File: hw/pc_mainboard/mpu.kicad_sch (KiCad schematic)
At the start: 0 parts

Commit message: Added MPU information
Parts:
- added U1: STM32MP151AABx, Package_BGA:ST_LFBGA-354_16x16mm_Layout19x19_P0.8mm, symbol MCU_ST_STM32MP1:STM32MP151AABx
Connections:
- new net: U1.A1 (VSS), U1.A19 (VSS), U1.B2 (VSS), U1.B6 (VSS), U1.C12 (VSS), U1.C13 (VSS), U1.C14 (VSS), U1.C15 (VSS), U1.C16 (VSS), U1.C17 (VSS), U1.C3 (VSS), U1.D1 (VSS), U1.D4 (VSS), U1.D5 (VSS), U1.D8 (VSS), U1.E10 (VSS), U1.E12 (VSS), U1.E14 (VSS), U1.E16 (VSS), U1.E2 (VSS), U1.E4 (VSS), U1.E5 (VSS), U1.E6 (VSS), U1.E8 (VSS), U1.F11 (VSS), U1.F15 (VSS), U1.F5 (VSS), U1.F7 (VSS), U1.F9 (VSS), U1.G10 (VSS), U1.G12 (VSS), U1.G14 (VSS), U1.G2 (VSS), U1.G4 (VSS), U1.G6 (VSS), U1.G8 (VSS), U1.H11 (VSS), U1.H13 (VSS), U1.H15 (VSS), U1.H5 (VSS), U1.H7 (VSS), U1.H9 (VSS), U1.J10 (VSS), U1.J12 (VSS), U1.J14 (VSS), U1.J3 (VSS), U1.J6 (VSS), U1.J8 (VSS), U1.K11 (VSS), U1.K13 (VSS), U1.K15 (VSS), U1.K2 (VSS), U1.K5 (VSS), U1.K7 (VSS), U1.K9 (VSS), U1.L10 (VSS), U1.L12 (VSS), U1.L14 (VSS), U1.L6 (VSS), U1.L8 (VSS), U1.M11 (VSS), U1.M13 (VSS), U1.M15 (VSS), U1.M5 (VSS), U1.M7 (VSS), U1.M9 (VSS), U1.N10 (VSS), U1.N12 (VSS), U1.N14 (VSS), U1.N6 (VSS), U1.N8 (VSS), U1.P11 (VSS), U1.P13 (VSS), U1.P15 (VSS), U1.P7 (VSS), U1.P9 (VSS), U1.R10 (VSS), U1.R12 (VSS), U1.R14 (VSS), U1.R16 (VSS), U1.R2 (VSS), U1.R6 (VSS), U1.R8 (VSS), U1.T4 (VSS), U1.U17 (VSS), U1.U3 (VSS), U1.U6 (VSS), U1.U8 (VSS), U1.W1 (VSS), U1.W19 (VSS)
- new net: U1.N4 (VSSA), U1.P5 (VSSA), U1.R5 (VSSA)
- new net: U1.U13 (VSS_USBHS), U1.U14 (VSS_USBHS), U1.V12 (VSS_USBHS), U1.V15 (VSS_USBHS)
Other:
- title: (none) -> MPU

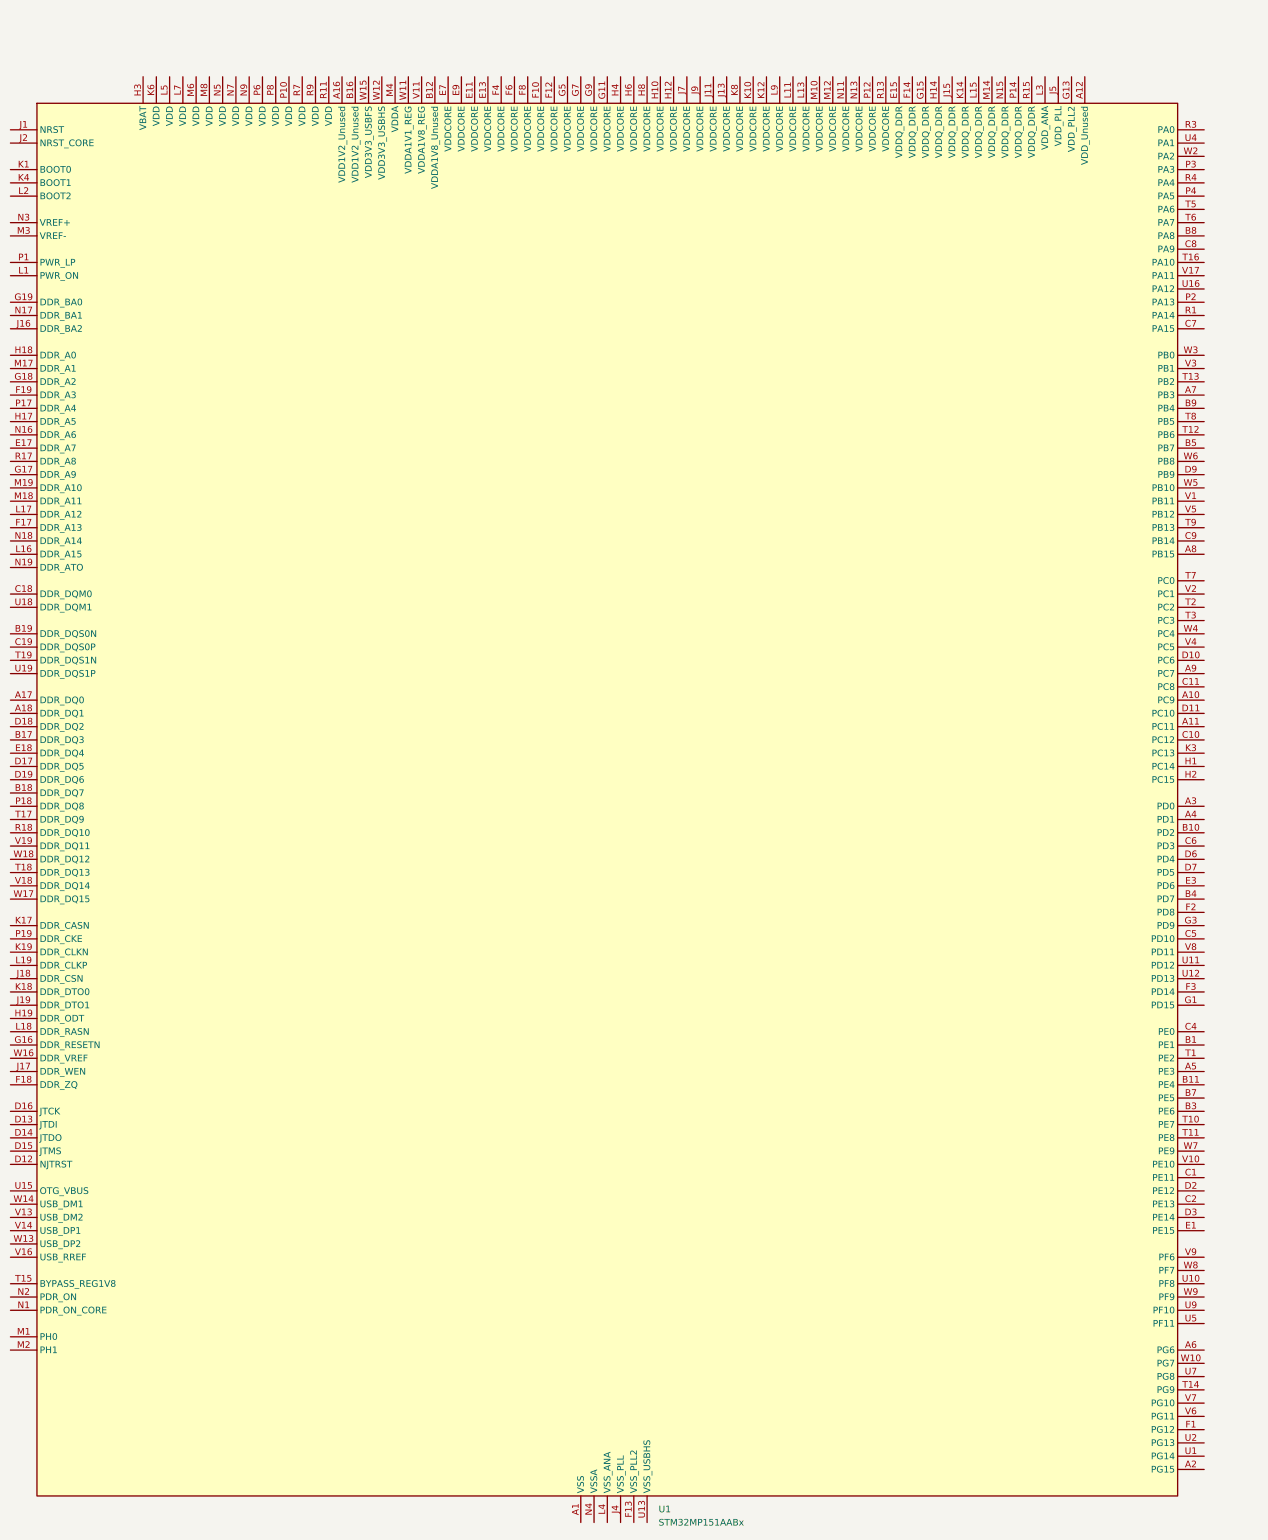
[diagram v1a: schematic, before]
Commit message: RAM Schematic Capture (#39)
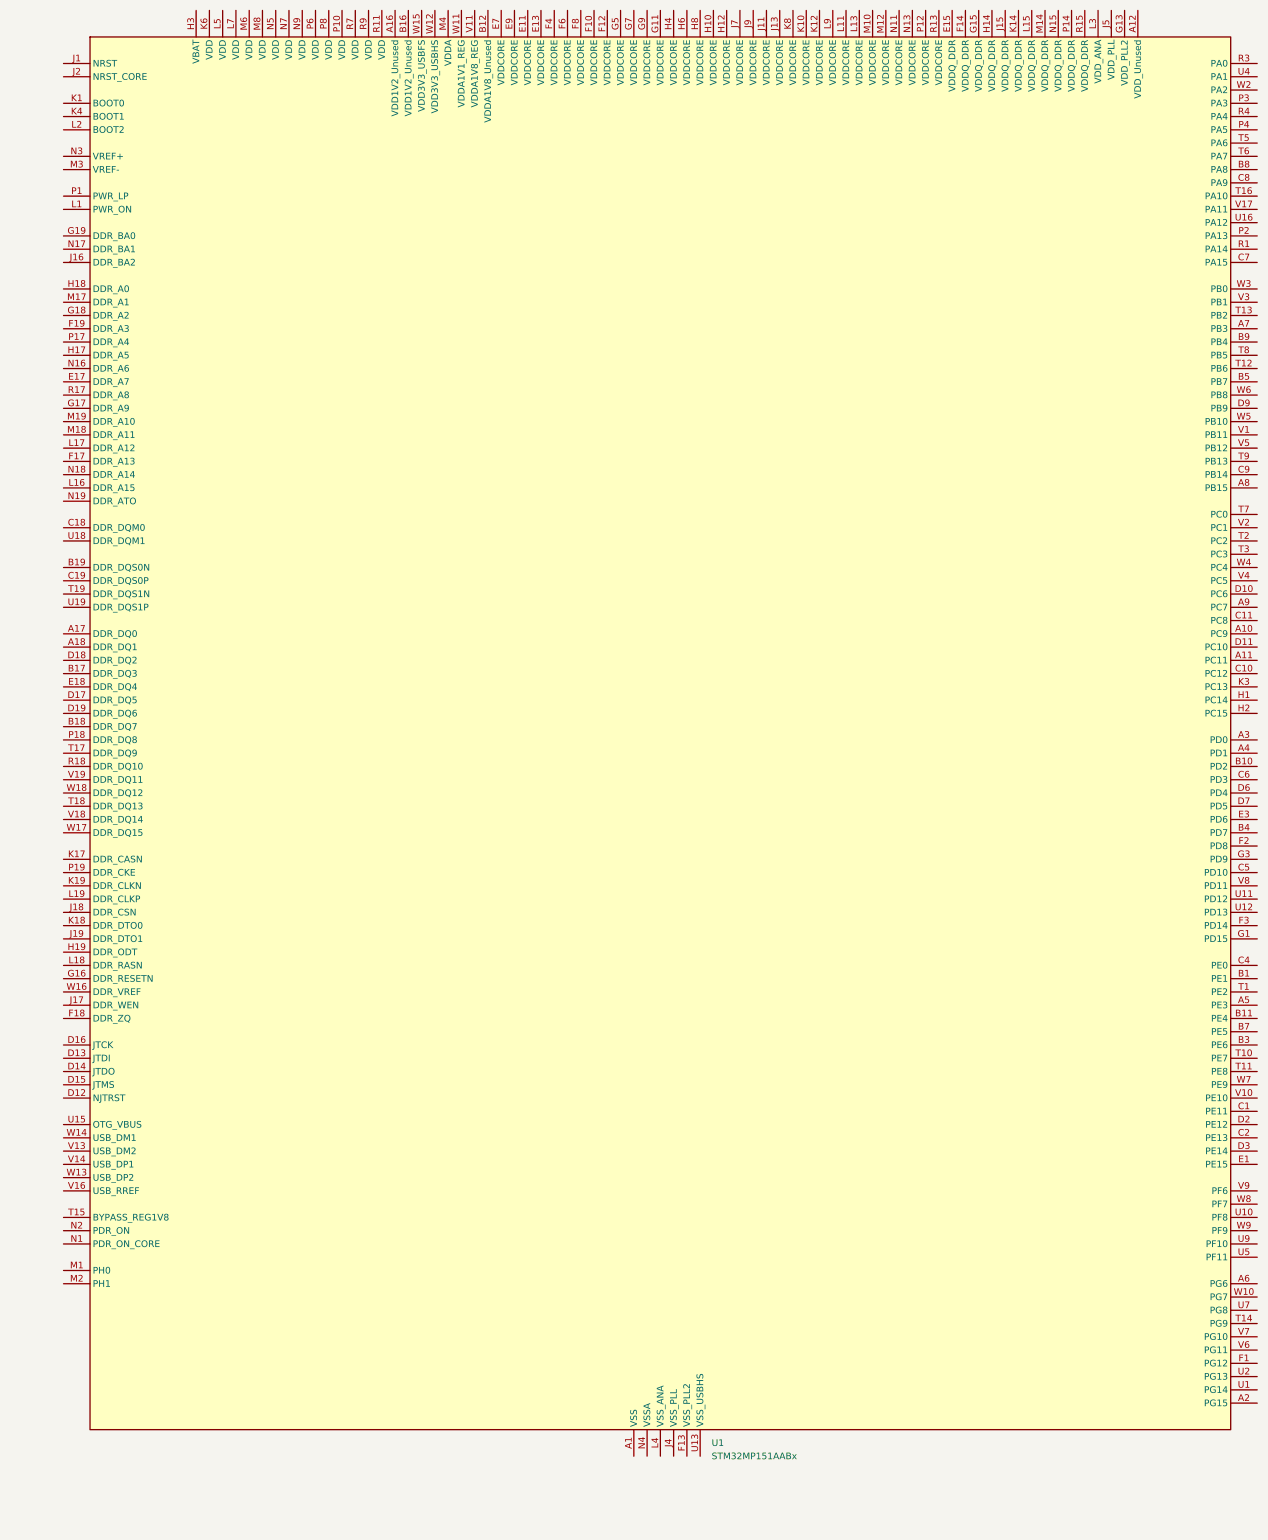
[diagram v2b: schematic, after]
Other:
- moved on the sheet: U1
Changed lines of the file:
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@@
 	(symbol
 		(lib_id "MCU_ST_STM32MP1:STM32MP151AABx")
-		(at 283.21 210.82 0)
+		(at 293.37 198.12 0)
 		(unit 1)
 		(exclude_from_sim no)
@@
 		(fields_autoplaced yes)
 		(property "Reference" "U1"
-			(at 293.0241 345.44 0)
+			(at 303.1841 332.74 0)
 			(effects
 				(font
@@
 		)
 		(property "Value" "STM32MP151AABx"
-			(at 293.0241 347.98 0)
+			(at 303.1841 335.28 0)
 			(effects
 				(font
@@
 		)
 		(property "Footprint" "Package_BGA:ST_LFBGA-354_16x16mm_Layout19x19_P0.8mm"
-			(at 173.99 342.9 0)
+			(at 184.15 330.2 0)
 			(effects
 				(font
@@
 		)
 		(property "Datasheet" "https://www.st.com/resource/en/datasheet/stm32mp151a.pdf"
-			(at 283.21 210.82 0)
+			(at 293.37 198.12 0)
 			(effects
 				(font
@@
 		)
 		(property "Description" "STMicroelectronics Arm Cortex-A7 MCU, 0KB flash, 708KB RAM, 98 GPIO, LFBGA354"
-			(at 283.21 210.82 0)
+			(at 293.37 198.12 0)
 			(effects
 				(font
